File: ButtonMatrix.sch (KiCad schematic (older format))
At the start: 138 parts, among them SW1 SW_Push_LED, SW10 SW_Push_LED, SW11 SW_Push_LED, SW12 SW_Push_LED, SW13 SW_Push_LED, SW14 SW_Push_LED, SW15 SW_Push_LED, SW16 SW_Push_LED, SW17 SW_Push_LED, SW18 SW_Push_LED, SW19 SW_Push_LED, SW2 SW_Push_LED, SW20 SW_Push_LED, SW21 SW_Push_LED, SW22 SW_Push_LED, SW23 SW_Push_LED, SW24 SW_Push_LED, SW25 SW_Push_LED, SW26 SW_Push_LED, SW27 SW_Push_LED, SW28 SW_Push_LED, SW29 SW_Push_LED, SW3 SW_Push_LED, SW30 SW_Push_LED, SW31 SW_Push_LED, SW32 SW_Push_LED, SW33 SW_Push_LED, SW34 SW_Push_LED, SW35 SW_Push_LED, SW36 SW_Push_LED, SW37 SW_Push_LED, SW38 SW_Push_LED, SW39 SW_Push_LED, SW4 SW_Push_LED, SW40 SW_Push_LED, SW41 SW_Push_LED, SW42 SW_Push_LED, SW43 SW_Push_LED, SW44 SW_Push_LED, SW45 SW_Push_LED, SW46 SW_Push_LED, SW47 SW_Push_LED, SW48 SW_Push_LED, SW49 SW_Push_LED, SW5 SW_Push_LED, SW50 SW_Push_LED, SW51 SW_Push_LED, SW52 SW_Push_LED, SW53 SW_Push_LED, SW54 SW_Push_LED, SW55 SW_Push_LED, SW56 SW_Push_LED, SW57 SW_Push_LED, SW58 SW_Push_LED, SW59 SW_Push_LED, SW6 SW_Push_LED, SW60 SW_Push_LED, SW61 SW_Push_LED, SW62 SW_Push_LED, SW63 SW_Push_LED, SW64 SW_Push_LED, SW65 SW_Push_LED, SW66 SW_Push_LED, SW67 SW_Push_LED, SW68 SW_Push_LED, SW69 SW_Push_LED, SW7 SW_Push_LED, SW8 SW_Push_LED, SW9 SW_Push_LED

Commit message: Add LED driver chip
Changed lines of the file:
@@
 Wire Wire Line
 	2050 2000 9200 2000
-Text HLabel 1950 2000 0    50   Input ~ 0
+Text HLabel 1950 2000 0    50   Output ~ 0
 ROW0
-Text HLabel 1950 2350 0    50   Input ~ 0
+Text HLabel 1950 2350 0    50   Output ~ 0
 ROW1
-Text HLabel 1950 2700 0    50   Input ~ 0
+Text HLabel 1950 2700 0    50   Output ~ 0
 ROW2
-Text HLabel 1950 3050 0    50   Input ~ 0
+Text HLabel 1950 3050 0    50   Output ~ 0
 ROW3
-Text HLabel 1950 3400 0    50   Input ~ 0
+Text HLabel 1950 3400 0    50   Output ~ 0
 ROW4
-Text HLabel 1950 3750 0    50   Input ~ 0
+Text HLabel 1950 3750 0    50   Output ~ 0
 ROW5
-Text HLabel 1950 4100 0    50   Input ~ 0
+Text HLabel 1950 4100 0    50   Output ~ 0
 ROW6
-Text HLabel 1950 4450 0    50   Input ~ 0
+Text HLabel 1950 4450 0    50   Output ~ 0
 ROW7
-Text HLabel 1950 4800 0    50   Input ~ 0
+Text HLabel 1950 4800 0    50   Output ~ 0
 ROW8
-Text HLabel 1950 5150 0    50   Input ~ 0
+Text HLabel 1950 5150 0    50   Output ~ 0
 ROW9
-Text HLabel 1950 5500 0    50   Input ~ 0
+Text HLabel 1950 5500 0    50   Output ~ 0
 ROW10
-Text HLabel 2650 1600 1    50   Output ~ 0
+Text HLabel 2650 1600 1    50   Input ~ 0
 COL0
-Text HLabel 3300 1600 1    50   Output ~ 0
+Text HLabel 3300 1600 1    50   Input ~ 0
 COL1
-Text HLabel 3950 1600 1    50   Output ~ 0
+Text HLabel 3950 1600 1    50   Input ~ 0
 COL2
-Text HLabel 4600 1600 1    50   Output ~ 0
+Text HLabel 4600 1600 1    50   Input ~ 0
 COL3
-Text HLabel 5250 1600 1    50   Output ~ 0
+Text HLabel 5250 1600 1    50   Input ~ 0
 COL4
-Text HLabel 5900 1600 1    50   Output ~ 0
+Text HLabel 5900 1600 1    50   Input ~ 0
 COL5
-Text HLabel 6550 1600 1    50   Output ~ 0
+Text HLabel 6550 1600 1    50   Input ~ 0
 COL6
-Text HLabel 7200 1600 1    50   Output ~ 0
+Text HLabel 7200 1600 1    50   Input ~ 0
 COL7
-Text HLabel 7850 1600 1    50   Output ~ 0
+Text HLabel 7850 1600 1    50   Input ~ 0
 COL8
-Text HLabel 8500 1600 1    50   Output ~ 0
+Text HLabel 8500 1600 1    50   Input ~ 0
 COL9
-Text HLabel 9150 1600 1    50   Output ~ 0
+Text HLabel 9150 1600 1    50   Input ~ 0
 COL10
-Text HLabel 9800 1550 1    50   Output ~ 0
+Text HLabel 9800 1550 1    50   Input ~ 0
 COL11
 $EndSCHEMATC

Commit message: Assign JLCPCB part numbers
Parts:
- D1, D10, D11, D12, D13, D14, D15, D16, D17, D18, D19, D2, D20, D21, D22, D23, D24, D25, D26, D27, D28, D29, D3, D30, D31, D32, D33, D34, D35, D36, D37, D38, D39, D4, D40, D41, D42, D43, D44, D45, D46, D47, D48, D49, D5, D50, D51, D52, D53, D54, D55, D56, D57, D58, D59, D6, D60, D61, D62, D63, D64, D65, D66, D67, D68, D69, D7, D8, D9: JLC (none) -> SOD-323F; LCSC (none) -> C2128

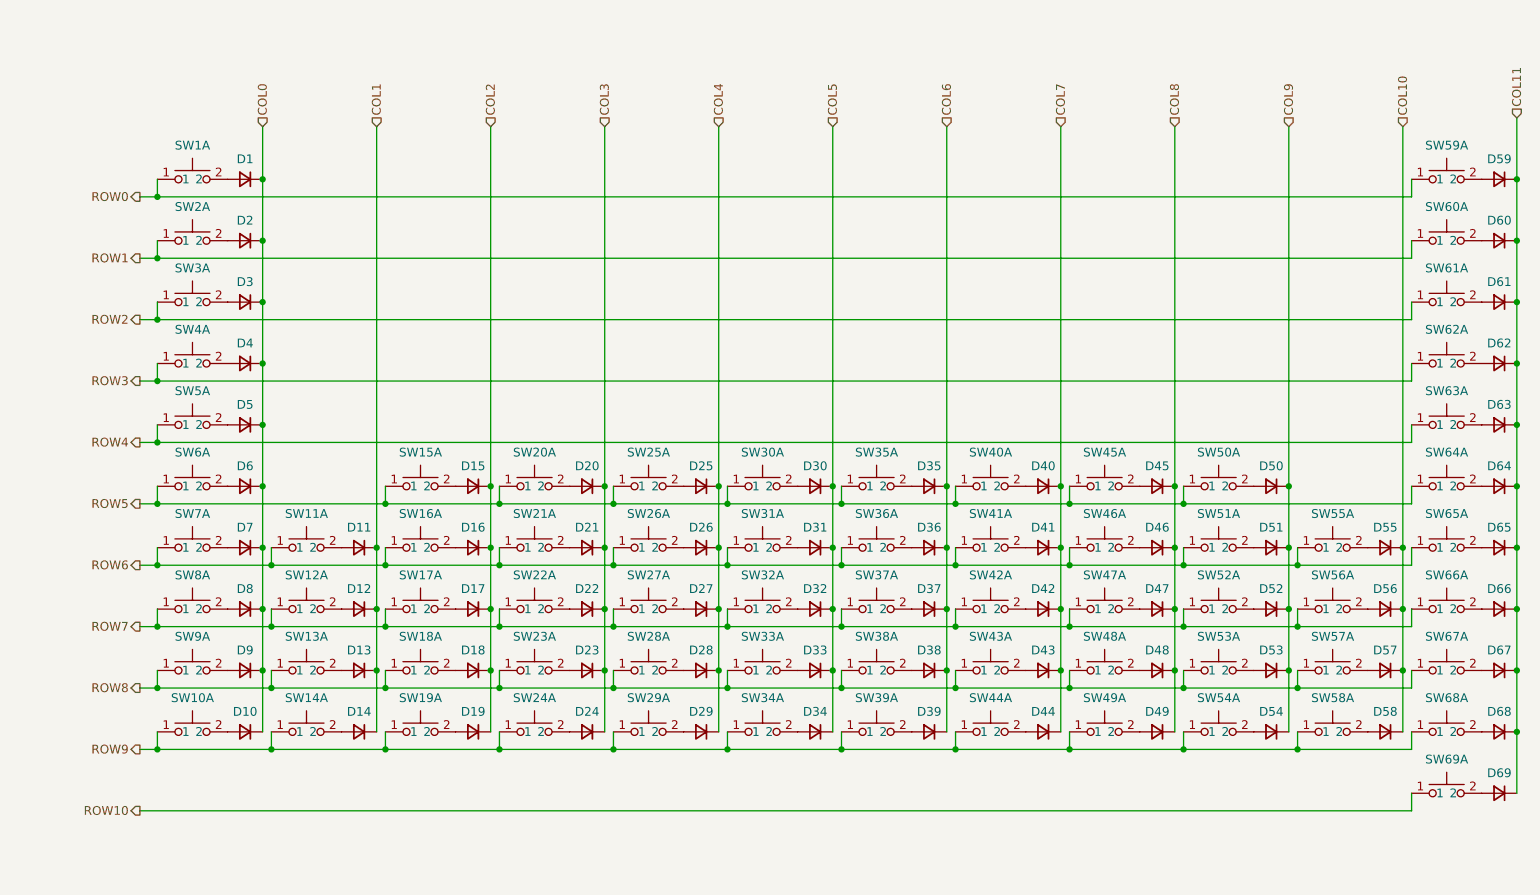
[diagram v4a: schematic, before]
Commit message: Fix the button layout. Still needs trace work.
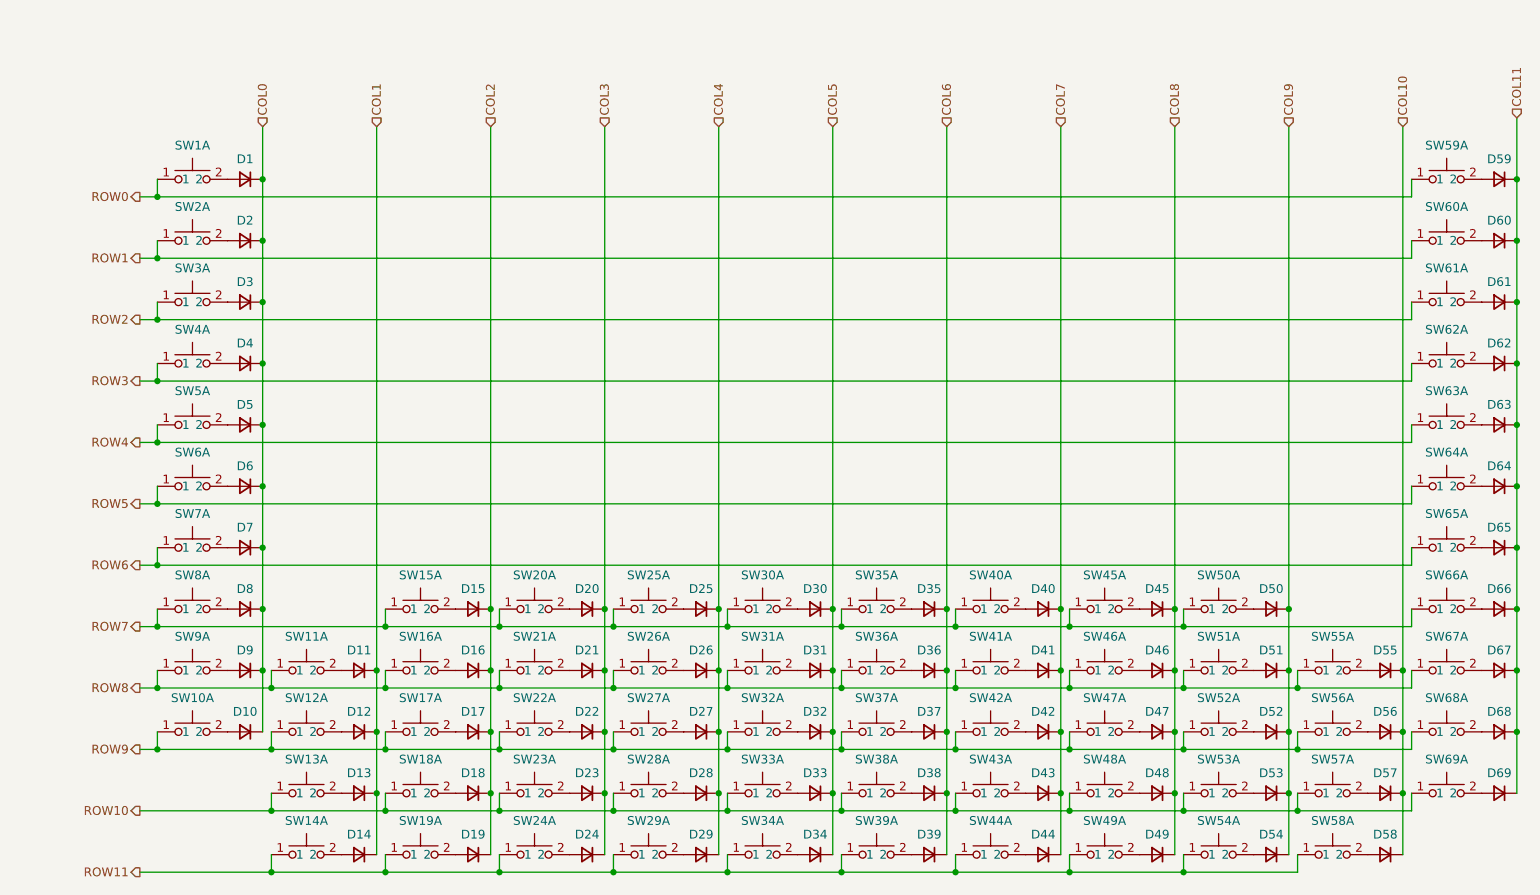
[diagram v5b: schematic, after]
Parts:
- removed D10, D68, D69, D9: D_Small, Diode_SMD:D_SOD-323F, symbol Device:D_Small
- removed SW10, SW68, SW69, SW9: SW_Push_LED, Collins-FMS-3000:SW_PUSH_6mm, symbol Collins-FMS-3000:SW_Push_LED
- added D6, D64, D65, D7: D_Small, Diode_SMD:D_SOD-323F, symbol Device:D_Small
- added SW6, SW64, SW65, SW7: SW_Push_LED, Collins-FMS-3000:SW_PUSH_6mm, symbol Collins-FMS-3000:SW_Push_LED
- renumbered D8 to D10, D64 to D66, D65 to D67, D66 to D68, D67 to D69, D6 to D8, D7 to D9, SW8 to SW10, SW64 to SW66, SW65 to SW67, SW66 to SW68, SW67 to SW69, SW6 to SW8, SW7 to SW9
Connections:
- net COL0: now also D6.1 (K), D7.1 (K)
- net COL11: now also D64.1 (K), D65.1 (K)
- net ROW10: now also SW13.1, SW18.1, SW23.1, SW28.1, SW33.1, SW38.1, SW43.1, SW48.1, SW53.1, SW57.1, SW69.1
- net ROW5: now also SW6.1, SW64.1; no longer SW15.1, SW20.1, SW25.1, SW30.1, SW35.1, SW40.1, SW45.1, SW50.1, SW66.1, SW8.1
- net ROW6: now also SW65.1, SW7.1; no longer SW11.1, SW16.1, SW21.1, SW26.1, SW31.1, SW36.1, SW41.1, SW46.1, SW51.1, SW55.1, SW67.1, SW9.1
- net ROW7: now also SW15.1, SW20.1, SW25.1, SW30.1, SW35.1, SW40.1, SW45.1, SW50.1, SW66.1, SW8.1; no longer SW10.1, SW12.1, SW17.1, SW22.1, SW27.1, SW32.1, SW37.1, SW42.1, SW47.1, SW52.1, SW56.1, SW68.1
- net ROW8: now also SW11.1, SW16.1, SW21.1, SW26.1, SW31.1, SW36.1, SW41.1, SW46.1, SW51.1, SW55.1, SW67.1, SW9.1; no longer SW13.1, SW18.1, SW23.1, SW28.1, SW33.1, SW38.1, SW43.1, SW48.1, SW53.1, SW57.1, SW69.1
- net ROW9: now also SW10.1, SW12.1, SW17.1, SW22.1, SW27.1, SW32.1, SW37.1, SW42.1, SW47.1, SW52.1, SW56.1, SW68.1; no longer SW14.1, SW19.1, SW24.1, SW29.1, SW34.1, SW39.1, SW44.1, SW49.1, SW54.1, SW58.1
- new net: D6.2 (A), SW6.2
- new net: D64.2 (A), SW64.2
- new net: D7.2 (A), SW7.2
- new net: D65.2 (A), SW65.2
- new net ROW11: SW14.1, SW19.1, SW24.1, SW29.1, SW34.1, SW39.1, SW44.1, SW49.1, SW54.1, SW58.1
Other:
- moved on the sheet: D10, D11, D12, D13, D14, D15, D16, D17, D18, D19, D20, D21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

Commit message: Remove diodes, update interrupt connections
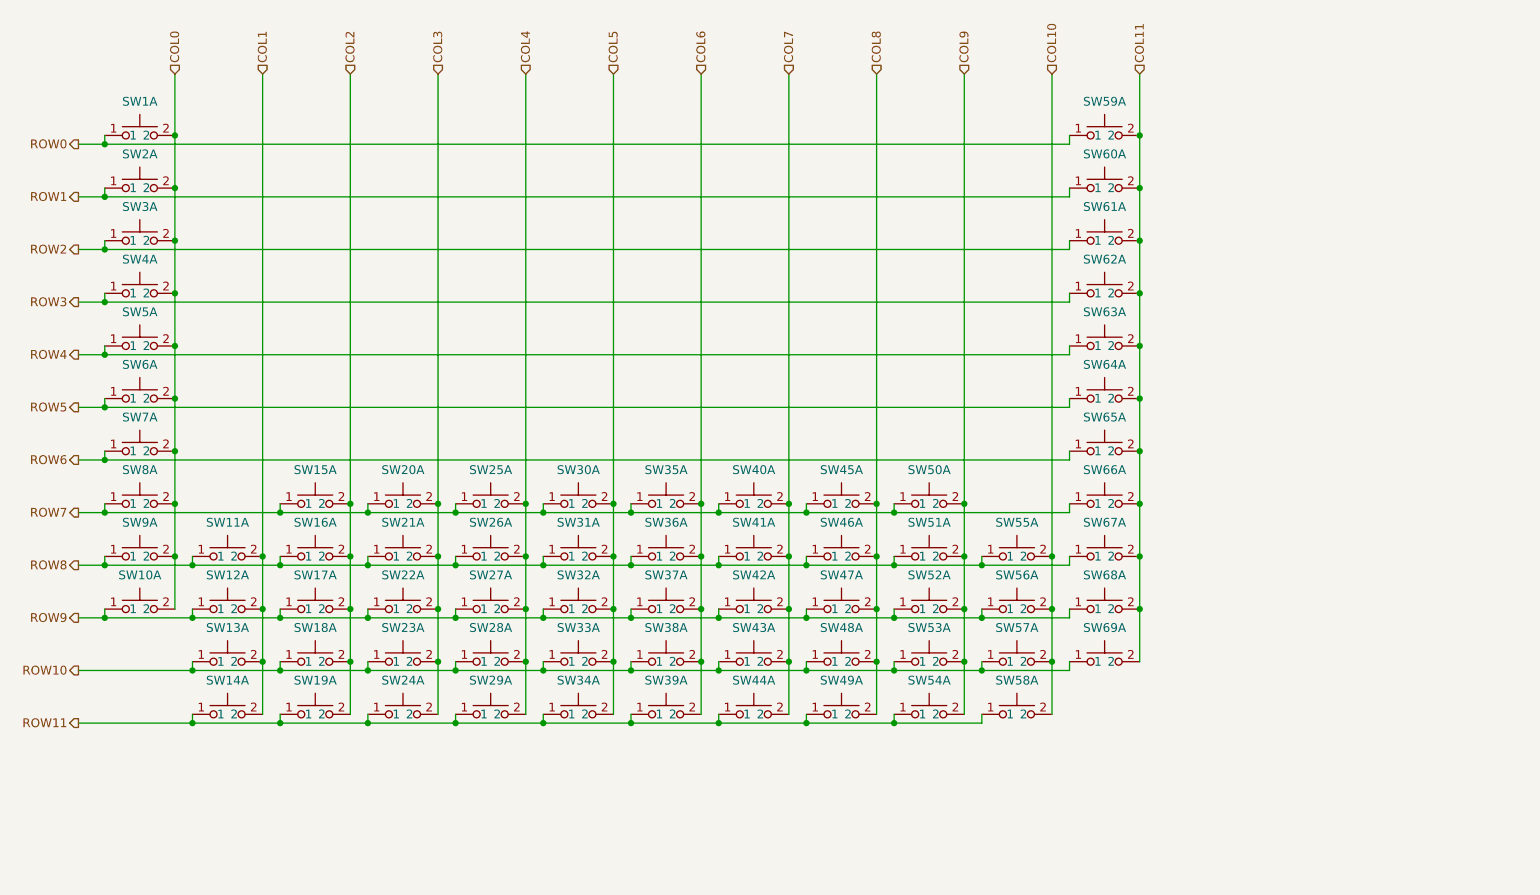
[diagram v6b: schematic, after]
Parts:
- removed D1, D10, D11, D12, D13, D14, D15, D16, D17, D18, D19, D2, D20, D21, D22, D23, D24, D25, D26, D27, D28, D29, D3, D30, D31, D32, D33, D34, D35, D36, D37, D38, D39, D4, D40, D41, D42, D43, D44, D45, D46, D47, D48, D49, D5, D50, D51, D52, D53, D54, D55, D56, D57, D58, D59, D6, D60, D61, D62, D63, D64, D65, D66, D67, D68, D69, D7, D8, D9: D_Small, Diode_SMD:D_SOD-323F, symbol Device:D_Small
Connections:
- net COL0: now also SW1.2, SW10.2, SW2.2, SW3.2, SW4.2, SW5.2, SW6.2, SW7.2, SW8.2, SW9.2
- net COL1: now also SW11.2, SW12.2, SW13.2, SW14.2
- net COL10: now also SW55.2, SW56.2, SW57.2, SW58.2
- net COL11: now also SW59.2, SW60.2, SW61.2, SW62.2, SW63.2, SW64.2, SW65.2, SW66.2, SW67.2, SW68.2, SW69.2
- net COL2: now also SW15.2, SW16.2, SW17.2, SW18.2, SW19.2
- net COL3: now also SW20.2, SW21.2, SW22.2, SW23.2, SW24.2
- net COL4: now also SW25.2, SW26.2, SW27.2, SW28.2, SW29.2
- net COL5: now also SW30.2, SW31.2, SW32.2, SW33.2, SW34.2
- net COL6: now also SW35.2, SW36.2, SW37.2, SW38.2, SW39.2
- net COL7: now also SW40.2, SW41.2, SW42.2, SW43.2, SW44.2
- net COL8: now also SW45.2, SW46.2, SW47.2, SW48.2, SW49.2
- net COL9: now also SW50.2, SW51.2, SW52.2, SW53.2, SW54.2

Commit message: Get rid of interrupt pullups, add row pullups
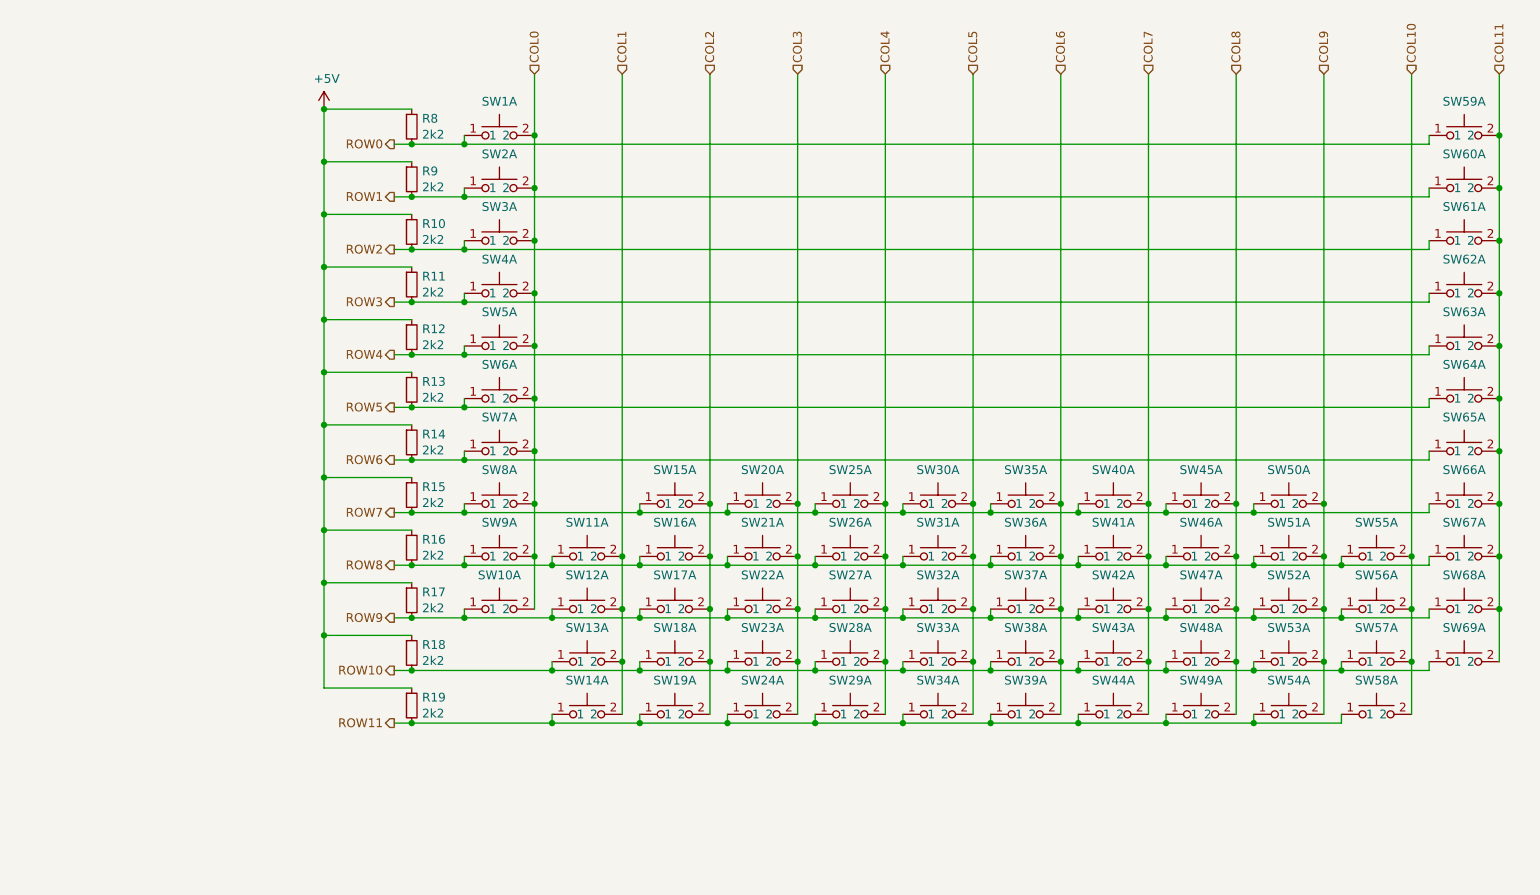
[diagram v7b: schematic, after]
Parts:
- added R10, R11, R12, R13, R14, R15, R16, R17, R18, R19, R8, R9: 2k2, Resistor_SMD:R_0402_1005Metric, symbol Device:R_Small
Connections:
- net ROW0: now also R8.2
- net ROW1: now also R9.2
- net ROW10: now also R18.2
- net ROW11: now also R19.2
- net ROW2: now also R10.2
- net ROW3: now also R11.2
- net ROW4: now also R12.2
- net ROW5: now also R13.2
- net ROW6: now also R14.2
- net ROW7: now also R15.2
- net ROW8: now also R16.2
- net ROW9: now also R17.2
- new net +5V: R10.1, R11.1, R12.1, R13.1, R14.1, R15.1, R16.1, R17.1, R18.1, R19.1, R8.1, R9.1
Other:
- moved on the sheet: SW10A, SW11A, SW12A, SW13A, SW14A, SW15A, SW16A, SW17A, SW18A, SW19A, SW1A, SW20A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

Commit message: Use perfect 0402 pad dimensions
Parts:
- R10, R11, R12, R13, R14, R15, R16, R17, R18, R19, R8, R9: footprint Resistor_SMD:R_0402_1005Metric -> Collins-FMS-3000:Perfect_0402
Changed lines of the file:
@@
 F 0 "R8" H 3559 1646 50  0000 L CNN
 F 1 "2k2" H 3559 1555 50  0000 L CNN
-F 2 "Resistor_SMD:R_0402_1005Metric" H 3500 1600 50  0001 C CNN
+F 2 "Collins-FMS-3000:Perfect_0402" H 3500 1600 50  0001 C CNN
 F 3 "~" H 3500 1600 50  0001 C CNN
 	1    3500 1600
@@
 F 0 "R9" H 3559 1946 50  0000 L CNN
 F 1 "2k2" H 3559 1855 50  0000 L CNN
-F 2 "Resistor_SMD:R_0402_1005Metric" H 3500 1900 50  0001 C CNN
+F 2 "Collins-FMS-3000:Perfect_0402" H 3500 1900 50  0001 C CNN
 F 3 "~" H 3500 1900 50  0001 C CNN
 	1    3500 1900
@@
 F 0 "R10" H 3559 2246 50  0000 L CNN
 F 1 "2k2" H 3559 2155 50  0000 L CNN
-F 2 "Resistor_SMD:R_0402_1005Metric" H 3500 2200 50  0001 C CNN
+F 2 "Collins-FMS-3000:Perfect_0402" H 3500 2200 50  0001 C CNN
 F 3 "~" H 3500 2200 50  0001 C CNN
 	1    3500 2200
@@
 F 0 "R11" H 3559 2546 50  0000 L CNN
 F 1 "2k2" H 3559 2455 50  0000 L CNN
-F 2 "Resistor_SMD:R_0402_1005Metric" H 3500 2500 50  0001 C CNN
+F 2 "Collins-FMS-3000:Perfect_0402" H 3500 2500 50  0001 C CNN
 F 3 "~" H 3500 2500 50  0001 C CNN
 	1    3500 2500
@@
 F 0 "R12" H 3559 2846 50  0000 L CNN
 F 1 "2k2" H 3559 2755 50  0000 L CNN
-F 2 "Resistor_SMD:R_0402_1005Metric" H 3500 2800 50  0001 C CNN
+F 2 "Collins-FMS-3000:Perfect_0402" H 3500 2800 50  0001 C CNN
 F 3 "~" H 3500 2800 50  0001 C CNN
 	1    3500 2800
@@
 F 0 "R13" H 3559 3146 50  0000 L CNN
 F 1 "2k2" H 3559 3055 50  0000 L CNN
-F 2 "Resistor_SMD:R_0402_1005Metric" H 3500 3100 50  0001 C CNN
+F 2 "Collins-FMS-3000:Perfect_0402" H 3500 3100 50  0001 C CNN
 F 3 "~" H 3500 3100 50  0001 C CNN
 	1    3500 3100
@@
 F 0 "R14" H 3559 3446 50  0000 L CNN
 F 1 "2k2" H 3559 3355 50  0000 L CNN
-F 2 "Resistor_SMD:R_0402_1005Metric" H 3500 3400 50  0001 C CNN
+F 2 "Collins-FMS-3000:Perfect_0402" H 3500 3400 50  0001 C CNN
 F 3 "~" H 3500 3400 50  0001 C CNN
 	1    3500 3400
@@
 F 0 "R15" H 3559 3746 50  0000 L CNN
 F 1 "2k2" H 3559 3655 50  0000 L CNN
-F 2 "Resistor_SMD:R_0402_1005Metric" H 3500 3700 50  0001 C CNN
+F 2 "Collins-FMS-3000:Perfect_0402" H 3500 3700 50  0001 C CNN
 F 3 "~" H 3500 3700 50  0001 C CNN
 	1    3500 3700
@@
 F 0 "R16" H 3559 4046 50  0000 L CNN
 F 1 "2k2" H 3559 3955 50  0000 L CNN
-F 2 "Resistor_SMD:R_0402_1005Metric" H 3500 4000 50  0001 C CNN
+F 2 "Collins-FMS-3000:Perfect_0402" H 3500 4000 50  0001 C CNN
 F 3 "~" H 3500 4000 50  0001 C CNN
 	1    3500 4000
@@
 F 0 "R17" H 3559 4346 50  0000 L CNN
 F 1 "2k2" H 3559 4255 50  0000 L CNN
-F 2 "Resistor_SMD:R_0402_1005Metric" H 3500 4300 50  0001 C CNN
+F 2 "Collins-FMS-3000:Perfect_0402" H 3500 4300 50  0001 C CNN
 F 3 "~" H 3500 4300 50  0001 C CNN
 	1    3500 4300
@@
 F 0 "R18" H 3559 4646 50  0000 L CNN
 F 1 "2k2" H 3559 4555 50  0000 L CNN
-F 2 "Resistor_SMD:R_0402_1005Metric" H 3500 4600 50  0001 C CNN
+F 2 "Collins-FMS-3000:Perfect_0402" H 3500 4600 50  0001 C CNN
 F 3 "~" H 3500 4600 50  0001 C CNN
 	1    3500 4600
@@
 F 0 "R19" H 3559 4946 50  0000 L CNN
 F 1 "2k2" H 3559 4855 50  0000 L CNN
-F 2 "Resistor_SMD:R_0402_1005Metric" H 3500 4900 50  0001 C CNN
+F 2 "Collins-FMS-3000:Perfect_0402" H 3500 4900 50  0001 C CNN
 F 3 "~" H 3500 4900 50  0001 C CNN
 	1    3500 4900
